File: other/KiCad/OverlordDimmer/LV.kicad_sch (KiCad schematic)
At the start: 93 parts, among them J3 Conn_01x12_Pin, U11 SN65HVD230

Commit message: sent to production
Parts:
- added 12VLED1, 3V3LED1, 5VLED1: LED, LED_SMD:LED_0805_2012Metric_Pad1.15x1.40mm_HandSolder, symbol Device:LED
- added R61: 60, Resistor_SMD:R_0805_2012Metric_Pad1.20x1.40mm_HandSolder, symbol Device:R
- added R67: 499, Resistor_SMD:R_0805_2012Metric_Pad1.20x1.40mm_HandSolder, symbol Device:R
- added R68: 147, Resistor_SMD:R_0805_2012Metric_Pad1.20x1.40mm_HandSolder, symbol Device:R
- renumbered C25 to C20, C20 to C21, C21 to C22, C22 to C23, C23 to C24, C24 to C25, JP4 to JP1, JP13 to JP10, JP14 to JP11, JP15 to JP12, JP16 to JP13, JP17 to JP14, JP18 to JP15, JP19 to JP16, JP20 to JP17, JP21 to JP18, JP22 to JP19, JP5 to JP2, JP23 to JP20, JP24 to JP21, JP25 to JP22, JP26 to JP23, JP27 to JP24, JP28 to JP25, JP29 to JP26, JP30 to JP27, JP31 to JP28, JP32 to JP29, JP6 to JP3, JP33 to JP30, JP34 to JP31, JP35 to JP32, JP36 to JP33, JP37 to JP34, JP38 to JP35, JP39 to JP36, JP40 to JP37, JP41 to JP38, JP42 to JP39, JP7 to JP4, JP43 to JP40, JP44 to JP41, JP45 to JP42, JP46 to JP43, JP47 to JP44, JP48 to JP45, JP49 to JP46, JP50 to JP47, JP51 to JP48, JP52 to JP49, JP8 to JP5, JP53 to JP50, JP54 to JP51, JP55 to JP52, JP56 to JP53, JP9 to JP6, JP10 to JP7, JP11 to JP8, JP12 to JP9, R61 to R62, R62 to R63, R63 to R64, R64 to R65, R65 to R66
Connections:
- net +12V: now also 12VLED1.2 (A)
- net +3.3V: now also 3V3LED1.2 (A)
- net +5V: now also 5VLED1.2 (A)
- net GND: now also R61.2, R67.2, R68.2
- new net: 5VLED1.1 (K), R68.1
- new net: 12VLED1.1 (K), R67.1
- new net: 3V3LED1.1 (K), R61.1
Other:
- moved on the sheet: C16, C17, D19, D20, D21, R58, R62, U_LM317_1

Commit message: sent to production with fixes
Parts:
- removed D20: 1N4148, Diode_SMD:D_0805_2012Metric_Pad1.15x1.40mm_HandSolder, symbol Diode:1N4148
- removed JP38, JP39, JP40, JP42, JP43, JP44, JP45, JP46, JP47, JP48, JP50, JP51, JP52, JP53: SolderJumper_2_Open, Jumper:SolderJumper-2_P1.3mm_Open_RoundedPad1.0x1.5mm, symbol Jumper:SolderJumper_2_Open
- removed J_JTAG1: FTSH-105-01-S-DV-K, OverlordCommon:FTSH-105-XX-YYY-DV-K, symbol FTSH-105-01-S-DV-K:FTSH-105-01-S-DV-K
- removed J_JTAG3V3_1, J_PROG3V3_1: Conn_01x02_Pin, Connector_PinHeader_2.54mm:PinHeader_1x02_P2.54mm_Vertical, symbol Connector:Conn_01x02_Pin
- removed R68: 147, Resistor_SMD:R_0805_2012Metric_Pad1.20x1.40mm_HandSolder, symbol Device:R
- added C26: 1uF, Capacitor_SMD:C_0805_2012Metric_Pad1.18x1.45mm_HandSolder, symbol Device:C
- added J4, J5: Conn_01x04_Pin, OverlordCommon:Solder_select_2x2, symbol Connector:Conn_01x04_Pin
- added J_JTAG2: FTSH-105-01-S-DV-K, OverlordCommon:FTSH-105-XX-YYY-DV-K, symbol FTSH-105-01-S-DV-K:FTSH-105-01-S-DV-K
- added R70: 147, Resistor_SMD:R_0805_2012Metric_Pad1.20x1.40mm_HandSolder, symbol Device:R
- added U_LM317_2: LM317_SOT-223, Package_TO_SOT_SMD:SOT-223-3_TabPin2, symbol Regulator_Linear:LM317_SOT-223
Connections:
- net +12V: now also C16.1, D19.1 (K), DB9_IN1.6, U_LM317_1.3 (VI); no longer DB9_IN1.9
- net +3.3V: now also D21.2 (A), JP41.2 (B), JP49.2 (B), U_LM317_2.2 (VO)
- net +5V: now also D21.1 (K), C26.1, U_LM317_2.3 (VI); no longer D21.2 (A)
- net CAN_H: now also DB9_IN1.8, J3.8 (Pin_8); no longer DB9_IN1.7
- net CAN_L: now also DB9_IN1.4, J3.9 (Pin_9); no longer DB9_IN1.2
- net ESP_EN: now also J_PROG1.1
- net ESP_IO0: now also J_PROG1.6
- net GND: now also DB9_IN1.5, J_PROG1.4, C26.2, J_JTAG2.3, J_JTAG2.5, J_JTAG2.7, J_JTAG2.9, R70.2; no longer DB9_IN1.1
- net JTAG_TCK: now also J_JTAG2.4; no longer JP41.2 (B)
- net JTAG_TDI: now also J_JTAG2.8
- net JTAG_TDO: now also J_JTAG2.6
- net JTAG_TMS: now also J_JTAG2.2
- net MB1_H: now also DB9_IN1.7; no longer DB9_IN1.8
- net MB1_L: now also DB9_IN1.9; no longer DB9_IN1.6
- net MB2_H: now also DB9_IN1.1; no longer DB9_IN1.5
- net MB2_L: now also DB9_IN1.2; no longer DB9_IN1.4
- net RS232_RX: now also J4.3 (Pin_3); no longer U_TRS3232EIPWR1.12 (ROUT1)
- net RS232_TX: now also J4.4 (Pin_4); no longer U_TRS3232EIPWR1.14 (DOUT1)
- net UART_RX_0: now also J_PROG1.5, J5.3 (Pin_3); no longer U_TRS3232EIPWR1.13 (RIN1)
- net UART_TX_0: now also J_PROG1.3, J5.4 (Pin_4); no longer U_TRS3232EIPWR1.11 (DIN1)
- net V_ADJ: now reaches R58.2, R62.1, U_LM317_1.1 (ADJ)
- net V_ADJ: now also U_LM317_2.1 (ADJ)
- net at 5VLED1.1 (K): now also R70.1
- net at JP41.1 (A): now also J_JTAG2.1
- new net: J4.1 (Pin_1), U_TRS3232EIPWR1.13 (RIN1)
- new net: J4.2 (Pin_2), U_TRS3232EIPWR1.14 (DOUT1)
- new net: J5.1 (Pin_1), U_TRS3232EIPWR1.11 (DIN1)
- new net: J5.2 (Pin_2), U_TRS3232EIPWR1.12 (ROUT1)
- no-connect marks 23 -> 21
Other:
- note added: "Power conversion 12V -> 3V3"
- note added: "Power conversion 5V -> 3V3"
- note removed: "Power conversion"
- moved on the sheet: 12VLED1, 3V3LED1, BOOT1, C13, C14, C16, C17, C18, C19, C20, C21, C22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

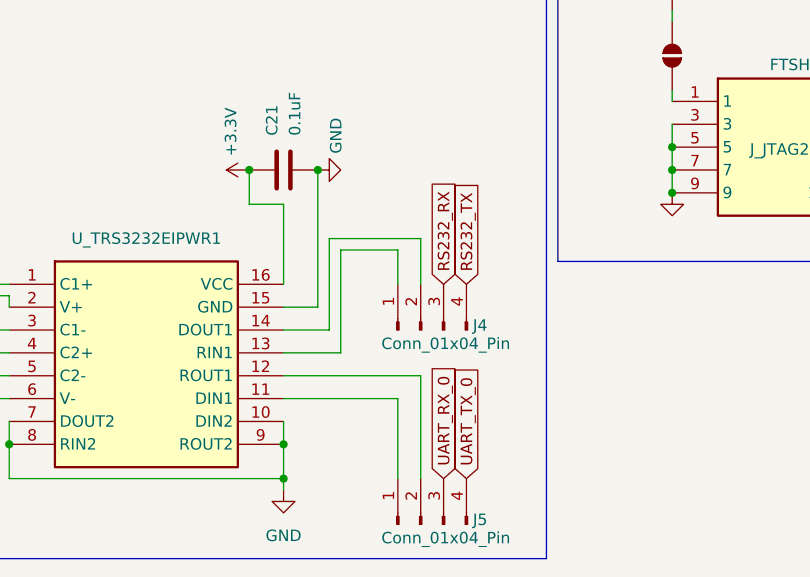
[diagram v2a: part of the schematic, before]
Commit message: update to latest rtdb_gen
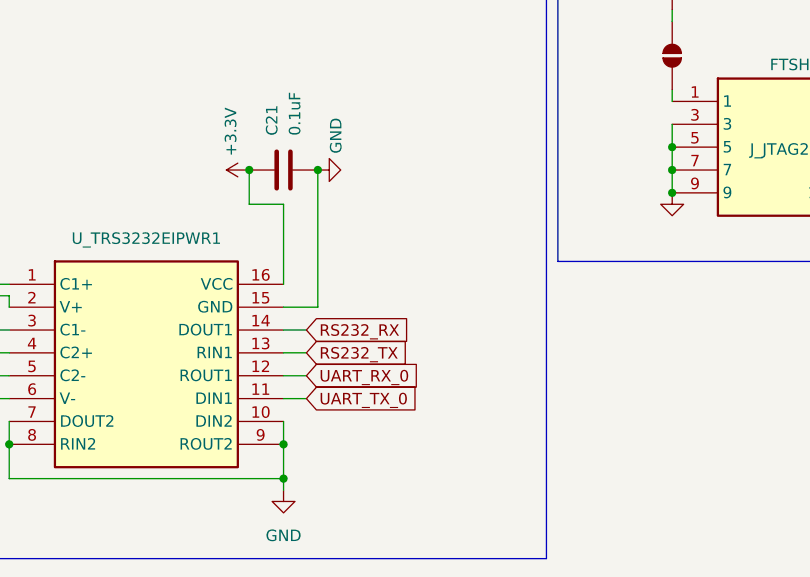
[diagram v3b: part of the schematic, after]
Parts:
- removed J4, J5: Conn_01x04_Pin, OverlordCommon:Solder_select_2x2, symbol Connector:Conn_01x04_Pin
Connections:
- net RS232_RX: now also U_TRS3232EIPWR1.14 (DOUT1)
- net RS232_TX: now also U_TRS3232EIPWR1.13 (RIN1)
- net UART_RX_0: now also U_TRS3232EIPWR1.12 (ROUT1)
- net UART_TX_0: now also U_TRS3232EIPWR1.11 (DIN1)
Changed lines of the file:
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@@
 	(wire
 		(pts
-			(xy 161.29 161.29) (xy 161.29 166.37)
-		)
-		(stroke
-			(width 0)
-			(type default)
-		)
-	)
-	(wire
-		(pts
 			(xy 200.66 26.67) (xy 200.66 31.75)
 		)
@@
 	(wire
 		(pts
-			(xy 146.05 179.07) (xy 158.75 179.07)
+			(xy 146.05 179.07) (xy 148.59 179.07)
 		)
 		(stroke
@@
 	(wire
 		(pts
-			(xy 152.4 173.99) (xy 152.4 162.56)
-		)
-		(stroke
-			(width 0)
-			(type default)
-		)
-	)
-	(wire
-		(pts
 			(xy 247.65 83.82) (xy 247.65 82.55)
 		)
@@
 	(wire
 		(pts
-			(xy 161.29 176.53) (xy 161.29 187.96)
-		)
-		(stroke
-			(width 0)
-			(type default)
-		)
-	)
-	(wire
-		(pts
 			(xy 265.43 43.18) (xy 264.16 43.18)
 		)
@@
 	(wire
 		(pts
-			(xy 146.05 176.53) (xy 161.29 176.53)
+			(xy 146.05 176.53) (xy 148.59 176.53)
 		)
 		(stroke
@@
 	(wire
 		(pts
-			(xy 146.05 173.99) (xy 152.4 173.99)
-		)
-		(stroke
-			(width 0)
-			(type default)
-		)
-	)
-	(wire
-		(pts
 			(xy 210.82 97.79) (xy 210.82 99.06)
 		)
@@
 	(wire
 		(pts
-			(xy 151.13 171.45) (xy 151.13 161.29)
-		)
-		(stroke
-			(width 0)
-			(type default)
-		)
-	)
-	(wire
-		(pts
-			(xy 146.05 171.45) (xy 151.13 171.45)
-		)
-		(stroke
-			(width 0)
-			(type default)
-		)
-	)
-	(wire
-		(pts
 			(xy 189.23 151.13) (xy 189.23 153.67)
 		)
@@
 	(wire
 		(pts
-			(xy 152.4 162.56) (xy 158.75 162.56)
-		)
-		(stroke
-			(width 0)
-			(type default)
-		)
-	)
-	(wire
-		(pts
 			(xy 137.16 54.61) (xy 137.16 52.07)
 		)
@@
 	(wire
 		(pts
-			(xy 151.13 161.29) (xy 161.29 161.29)
-		)
-		(stroke
-			(width 0)
-			(type default)
-		)
-	)
-	(wire
-		(pts
 			(xy 118.11 125.73) (xy 118.11 127)
 		)
@@
 	(wire
 		(pts
-			(xy 232.41 83.82) (xy 232.41 82.55)
+			(xy 146.05 171.45) (xy 148.59 171.45)
 		)
 		(stroke
@@
 	(wire
 		(pts
-			(xy 185.42 38.1) (xy 185.42 31.75)
+			(xy 232.41 83.82) (xy 232.41 82.55)
 		)
 		(stroke
@@
 		)
 	)
-	(polyline
+	(wire
 		(pts
-			(xy 96.52 13.97) (xy 175.26 13.97)
+			(xy 185.42 38.1) (xy 185.42 31.75)
 		)
 		(stroke
@@
 	(polyline
 		(pts
-			(xy 175.26 133.35) (xy 96.52 133.35)
+			(xy 96.52 13.97) (xy 175.26 13.97)
 		)
 		(stroke
@@
 		)
 	)
-	(wire
+	(polyline
 		(pts
-			(xy 234.95 83.82) (xy 234.95 82.55)
+			(xy 175.26 133.35) (xy 96.52 133.35)
 		)
 		(stroke
@@
 	(wire
 		(pts
-			(xy 158.75 179.07) (xy 158.75 187.96)
+			(xy 234.95 83.82) (xy 234.95 82.55)
 		)
 		(stroke
@@
 	(wire
 		(pts
-			(xy 158.75 162.56) (xy 158.75 166.37)
+			(xy 200.66 45.72) (xy 201.93 45.72)
 		)
 		(stroke
@@
 	(wire
 		(pts
-			(xy 200.66 45.72) (xy 201.93 45.72)
+			(xy 35.56 186.69) (xy 35.56 185.42)
 		)
 		(stroke
@@
 	(wire
 		(pts
-			(xy 35.56 186.69) (xy 35.56 185.42)
+			(xy 269.24 154.94) (xy 264.16 154.94)
 		)
 		(stroke
@@
 	(wire
 		(pts
-			(xy 269.24 154.94) (xy 264.16 154.94)
+			(xy 256.54 35.56) (xy 267.97 35.56)
 		)
 		(stroke
@@
 	(wire
 		(pts
-			(xy 256.54 35.56) (xy 267.97 35.56)
+			(xy 265.43 45.72) (xy 264.16 45.72)
 		)
 		(stroke
@@
 	(wire
 		(pts
-			(xy 265.43 45.72) (xy 264.16 45.72)
+			(xy 146.05 173.99) (xy 148.59 173.99)
 		)
 		(stroke
@@
 	(global_label "UART_TX_0"
 		(shape input)
-		(at 166.37 187.96 90)
+		(at 148.59 179.07 0)
 		(effects
 			(font
@@
 		)
 		(property "Intersheetrefs" "${INTERSHEET_REFS}"
-			(at 166.37 187.96 0)
+			(at 148.59 179.07 0)
 			(effects
 				(font
@@
 	(global_label "RS232_TX"
 		(shape input)
-		(at 166.37 166.37 90)
+		(at 148.59 173.99 0)
 		(fields_autoplaced yes)
 		(effects
@@
 		)
 		(property "Intersheetrefs" "${INTERSHEET_REFS}"
-			(at 166.37 154.1321 90)
+			(at 160.8279 173.99 0)
 			(effects
 				(font
@@
 	(global_label "RS232_RX"
 		(shape input)
-		(at 163.83 166.37 90)
+		(at 148.59 171.45 0)
 		(fields_autoplaced yes)
 		(effects
@@
 		)
 		(property "Intersheetrefs" "${INTERSHEET_REFS}"
-			(at 163.83 153.8297 90)
+			(at 161.1303 171.45 0)
 			(effects
 				(font
@@
 	(global_label "UART_RX_0"
 		(shape input)
-		(at 163.83 187.96 90)
+		(at 148.59 176.53 0)
 		(effects
 			(font
@@
 		)
 		(property "Intersheetrefs" "${INTERSHEET_REFS}"
-			(at 163.83 187.96 0)
+			(at 148.59 176.53 0)
 			(effects
 				(font
@@
 	)
 	(symbol
-		(lib_id "Connector:Conn_01x04_Pin")
-		(at 161.29 171.45 90)
-		(unit 1)
-		(exclude_from_sim no)
-		(in_bom yes)
-		(on_board yes)
-		(dnp no)
-		(property "Reference" "J4"
-			(at 167.894 170.942 90)
-			(effects
-				(font
-					(size 1.27 1.27)
-				)
-			)
-		)
-		(property "Value" "Conn_01x04_Pin"
-			(at 164.084 172.974 90)
-			(effects
-				(font
-					(size 1.27 1.27)
-				)
-			)
-		)
-		(property "Footprint" "OverlordCommon:Solder_select_2x2"
-			(at 161.29 171.45 0)
-			(effects
-				(font
-					(size 1.27 1.27)
-				)
-				(hide yes)
-			)
-		)
-		(property "Datasheet" "~"
-			(at 161.29 171.45 0)
-			(effects
-				(font
-					(size 1.27 1.27)
-				)
-				(hide yes)
-			)
-		)
-		(property "Description" "Generic connector, single row, 01x04, script generated"
-			(at 161.29 171.45 0)
-			(effects
-				(font
-					(size 1.27 1.27)
-				)
-				(hide yes)
-			)
-		)
-		(pin "1"
-		)
-		(pin "4"
-		)
-		(pin "2"
-		)
-		(pin "3"
-		)
-		(instances
-			(project ""
-				(path "/61f84ae7-a90a-49d4-ad4c-9c4f7abf6876/1999b2f3-c135-4e2b-81b7-cc4e1321536b"
-					(reference "J4")
-					(unit 1)
-				)
-			)
-		)
-	)
-	(symbol
 		(lib_id "power:+3.3V")
 		(at 274.32 152.4 0)
@@
 					(unit 1)
 				)
-			)
-		)
-	)
-	(symbol
-		(lib_id "Connector:Conn_01x04_Pin")
-		(at 161.29 193.04 90)
-		(unit 1)
-		(exclude_from_sim no)
-		(in_bom yes)
-		(on_board yes)
-		(dnp no)
-		(property "Reference" "J5"
-			(at 167.894 192.532 90)
-			(effects
-				(font
-					(size 1.27 1.27)
-				)
-			)
-		)
-		(property "Value" "Conn_01x04_Pin"
-			(at 164.084 194.564 90)
-			(effects
-				(font
-					(size 1.27 1.27)
-				)
-			)
-		)
-		(property "Footprint" "OverlordCommon:Solder_select_2x2"
-			(at 161.29 193.04 0)
-			(effects
-				(font
-					(size 1.27 1.27)
-				)
-				(hide yes)
-			)
-		)
-		(property "Datasheet" "~"
-			(at 161.29 193.04 0)
-			(effects
-				(font
-					(size 1.27 1.27)
-				)
-				(hide yes)
-			)
-		)
-		(property "Description" "Generic connector, single row, 01x04, script generated"
-			(at 161.29 193.04 0)
-			(effects
-				(font
-					(size 1.27 1.27)
-				)
-				(hide yes)
-			)
-		)
-		(pin "1"
-		)
-		(pin "4"
-		)
-		(pin "2"
-		)
-		(pin "3"
-		)
-		(instances
-			(project "OverlordDimmer"
-				(path "/61f84ae7-a90a-49d4-ad4c-9c4f7abf6876/1999b2f3-c135-4e2b-81b7-cc4e1321536b"
-					(reference "J5")
-					(unit 1)
-				)

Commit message: Sent for PCB production, ver 1.2 rev A
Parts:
- removed 12VLED1, 3V3LED1, 5VLED1: LED, LED_SMD:LED_0805_2012Metric_Pad1.15x1.40mm_HandSolder, symbol Device:LED
- removed C16, C17, C26: 1uF, Capacitor_SMD:C_0805_2012Metric_Pad1.18x1.45mm_HandSolder, symbol Device:C
- removed D19, D21: 1N4148, Diode_SMD:D_0805_2012Metric_Pad1.15x1.40mm_HandSolder, symbol Diode:1N4148
- removed JP41, JP49: SolderJumper_2_Open, Jumper:SolderJumper-2_P1.3mm_Open_RoundedPad1.0x1.5mm, symbol Jumper:SolderJumper_2_Open
- removed J_USB1: USB_B, Connector_USB:USB_B_Lumberg_2411_02_Horizontal, symbol Connector:USB_B
- removed R58: 240, Resistor_SMD:R_0805_2012Metric, symbol Device:R
- removed R61: 60, Resistor_SMD:R_0805_2012Metric_Pad1.20x1.40mm_HandSolder, symbol Device:R
- removed R62: 390, Resistor_SMD:R_0805_2012Metric, symbol Device:R
- removed R67: 499, Resistor_SMD:R_0805_2012Metric_Pad1.20x1.40mm_HandSolder, symbol Device:R
- removed R70: 147, Resistor_SMD:R_0805_2012Metric_Pad1.20x1.40mm_HandSolder, symbol Device:R
- removed U_LM317_1, U_LM317_2: LM317_SOT-223, Package_TO_SOT_SMD:SOT-223-3_TabPin2, symbol Regulator_Linear:LM317_SOT-223
- added J4: USB_B_Micro, Connector_USB:USB_Micro-B_Wuerth_614105150721_Vertical_CircularHoles, symbol Connector:USB_B_Micro
- added J5: I2C, Connector_PinHeader_1.27mm:PinHeader_1x04_P1.27mm_Vertical, symbol Connector:Conn_01x04_Socket
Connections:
- net +3.3V: now also J_JTAG2.1, J_PROG1.2, J5.4 (Pin_4)
- net +5V: now also J4.1 (VBUS)
- net D+: now also J4.3 (D+)
- net D-: now also J4.2 (D-)
- net EDGE_DETECT: now also JP19.2 (B); no longer JP17.2 (B)
- net GND: now also J4.5 (GND), J4.6 (Shield), J5.1 (Pin_1)
- net SCL: now reaches JP3.2 (B)
- net SCL: now also J5.2 (Pin_2)
- net SDA: now reaches JP1.2 (B)
- net SDA: now also J5.3 (Pin_3)
- new net UNDERV_DETECT: JP17.2 (B)
- no-connect marks 21 -> 19
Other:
- added sheet Power conversion (PowerConversion.kicad_sch)
- note removed: "390 Ohm - 3.3V 680 Ohm - 5V"
- note removed: "Power conversion 12V -> 3V3"
- note removed: "Power conversion 5V -> 3V3"
- moved on the sheet: C20, C21, C22, C23, C24, C25, D22, J3, U_TRS3232EIPWR1

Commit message: Updated PCB design - added pullup on boot pin GPIO0 - schematic cleanup - removed unused power supply parts
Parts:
- removed C18: 0.1uF, Capacitor_SMD:C_0805_2012Metric_Pad1.18x1.45mm_HandSolder, symbol Device:C
- added C12: 22uF, Capacitor_SMD:C_0805_2012Metric_Pad1.18x1.45mm_HandSolder, symbol Device:C
- added R73: 10k, Resistor_SMD:R_0805_2012Metric_Pad1.20x1.40mm_HandSolder, symbol Device:R
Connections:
- net +3.3V: now also R73.2
- net ESP_EN: now also C12.1
- net ESP_IO0: now also R73.1
- net GND: now also C12.2
- net +5V renamed USB+5V
- net MB1_H renamed MB1_A
- net MB1_L renamed MB1_B
- net MB2_H renamed MB2_A
- net MB2_L renamed MB2_B
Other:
- moved on the sheet: BOOT1, C19, R66, RESET1
